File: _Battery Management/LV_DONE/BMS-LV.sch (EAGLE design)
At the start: 114 parts, among them J1 M1x5, J2 M1x4, J3 M1x4, J4 M1x4, J5 M1x2, J6 MX150L, J8 M1x5, J9 M80022232081-2, K1 ADJ14024, Q2 40V 0.2A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

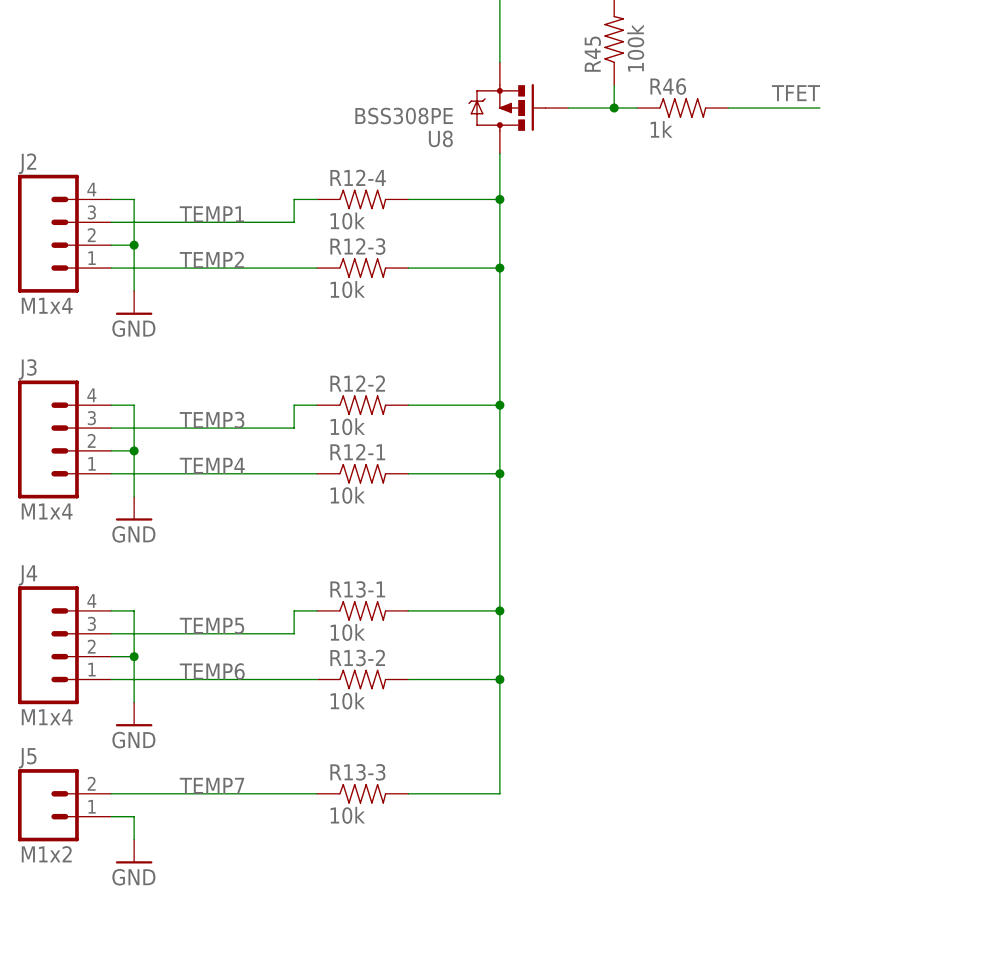
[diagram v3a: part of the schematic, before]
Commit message: Fixing layout issues.
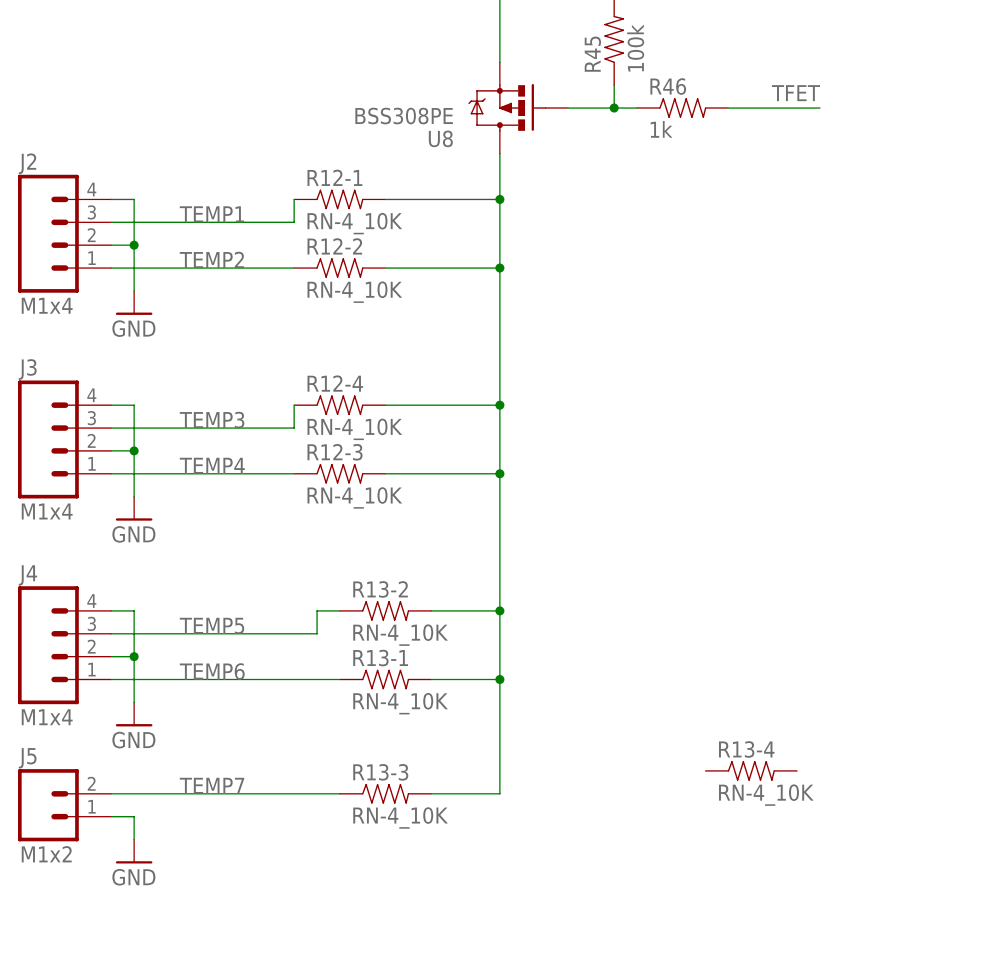
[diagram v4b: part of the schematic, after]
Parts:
- R12, R13: value 10k -> RN-4_10K
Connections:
- net TEMP1: now also R12-1.1; no longer R12-4.1
- net TEMP2: now also R12-2.1; no longer R12-3.1
- net TEMP3: now also R12-4.1; no longer R12-2.1
- net TEMP4: now also R12-3.1; no longer R12-1.1
- net TEMP5: now also R13-2.1; no longer R13-1.1
- net TEMP6: now also R13-1.1; no longer R13-2.1
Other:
- moved on the sheet: R12-1, R12-2, R12-3, R12-4, R13-1, R13-2, R13-3
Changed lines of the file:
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@@
 <part name="J3" library="FSAE Electric" deviceset="M4" device="_1X4_LOCK" value="M1x4"/>
 <part name="J4" library="FSAE Electric" deviceset="M4" device="_1X4_LOCK" value="M1x4"/>
-<part name="R13" library="FSAE Electric" deviceset="RN-4" device="_10K" value="10k"/>
 <part name="GND6" library="supply1" deviceset="GND" device=""/>
 <part name="GND16" library="supply1" deviceset="GND" device=""/>
@@
 <part name="J6" library="FSAE Electric" deviceset="M2X3" device="MX150L" value="MX150L"/>
 <part name="C1" library="FSAE Electric" deviceset="CAP" device="_0.1UF_50V" value="0.1uF"/>
-<part name="R12" library="FSAE Electric" deviceset="RN-4" device="_10K" value="10k"/>
 <part name="J9" library="FSAE Electric" deviceset="M8" device="0022232081-2"/>
 <part name="R50" library="FSAE Electric" deviceset="RES" device="_4.99K_1%" value="4.99k"/>
@@
 <part name="R58" library="FSAE Electric" deviceset="RES" device="_10K_1%" value="10k"/>
 <part name="P+4" library="supply1" deviceset="+5V" device=""/>
+<part name="R12" library="FSAE Electric" deviceset="RN-4" device="_10K"/>
+<part name="R13" library="FSAE Electric" deviceset="RN-4" device="_10K"/>
 </parts>
 <sheets>
@@
 <instance part="J3" gate="G$1" x="22.86" y="68.58"/>
 <instance part="J4" gate="G$1" x="22.86" y="45.72"/>
-<instance part="R13" gate="-1" x="55.88" y="45.72"/>
-<instance part="R13" gate="-2" x="55.88" y="38.1"/>
-<instance part="R13" gate="-3" x="55.88" y="25.4"/>
 <instance part="GND6" gate="1" x="30.48" y="78.74"/>
 <instance part="GND16" gate="1" x="30.48" y="55.88"/>
@@
 <attribute name="VALUE" x="55.88" y="243.84" size="1.778" layer="96"/>
 </instance>
-<instance part="R12" gate="-1" x="55.88" y="60.96"/>
-<instance part="R12" gate="-2" x="55.88" y="68.58"/>
-<instance part="R12" gate="-3" x="55.88" y="83.82"/>
-<instance part="R12" gate="-4" x="55.88" y="91.44"/>
 <instance part="J9" gate="G$1" x="231.14" y="177.8"/>
 <instance part="R50" gate="G$1" x="441.96" y="200.66" rot="R90"/>
@@
 <attribute name="VALUE" x="462.28" y="182.88" size="1.778" layer="96" rot="R90"/>
 </instance>
+<instance part="R12" gate="-1" x="53.34" y="91.44"/>
+<instance part="R12" gate="-2" x="53.34" y="83.82"/>
+<instance part="R12" gate="-3" x="53.34" y="60.96"/>
+<instance part="R12" gate="-4" x="53.34" y="68.58"/>
+<instance part="R13" gate="-1" x="58.42" y="38.1"/>
+<instance part="R13" gate="-2" x="58.42" y="45.72"/>
+<instance part="R13" gate="-3" x="58.42" y="25.4"/>
+<instance part="R13" gate="-4" x="99.06" y="27.94"/>
 </instances>
 <busses>
@@
 </segment>
 <segment>
-<wire x1="50.8" y1="91.44" x2="48.26" y2="91.44" width="0.1524" layer="91"/>
-<wire x1="48.26" y1="91.44" x2="48.26" y2="88.9" width="0.1524" layer="91"/>
 <pinref part="J2" gate="G$1" pin="3"/>
 <wire x1="48.26" y1="88.9" x2="27.94" y2="88.9" width="0.1524" layer="91"/>
 <label x="35.56" y="88.9" size="1.778" layer="95"/>
-<pinref part="R12" gate="-4" pin="1"/>
+<pinref part="R12" gate="-1" pin="1"/>
+<wire x1="48.26" y1="88.9" x2="48.26" y2="91.44" width="0.1524" layer="91"/>
 </segment>
 </net>
@@
 </segment>
 <segment>
-<wire x1="50.8" y1="68.58" x2="48.26" y2="68.58" width="0.1524" layer="91"/>
-<wire x1="48.26" y1="68.58" x2="48.26" y2="66.04" width="0.1524" layer="91"/>
 <pinref part="J3" gate="G$1" pin="3"/>
 <wire x1="48.26" y1="66.04" x2="27.94" y2="66.04" width="0.1524" layer="91"/>
 <label x="35.56" y="66.04" size="1.778" layer="95"/>
-<pinref part="R12" gate="-2" pin="1"/>
+<pinref part="R12" gate="-4" pin="1"/>
+<wire x1="48.26" y1="66.04" x2="48.26" y2="68.58" width="0.1524" layer="91"/>
 </segment>
 </net>
@@
 </segment>
 <segment>
-<wire x1="48.26" y1="45.72" x2="48.26" y2="43.18" width="0.1524" layer="91"/>
 <pinref part="J4" gate="G$1" pin="3"/>
-<wire x1="48.26" y1="43.18" x2="27.94" y2="43.18" width="0.1524" layer="91"/>
+<wire x1="50.8" y1="45.72" x2="50.8" y2="43.18" width="0.1524" layer="91"/>
+<wire x1="50.8" y1="43.18" x2="27.94" y2="43.18" width="0.1524" layer="91"/>
 <label x="35.56" y="43.18" size="1.778" layer="95"/>
-<pinref part="R13" gate="-1" pin="1"/>
-<wire x1="48.26" y1="45.72" x2="50.8" y2="45.72" width="0.1524" layer="91"/>
+<pinref part="R13" gate="-2" pin="1"/>
+<wire x1="50.8" y1="45.72" x2="53.34" y2="45.72" width="0.1524" layer="91"/>
 </segment>
 </net>
@@
 <segment>
 <pinref part="J2" gate="G$1" pin="1"/>
-<wire x1="50.8" y1="83.82" x2="27.94" y2="83.82" width="0.1524" layer="91"/>
+<wire x1="48.26" y1="83.82" x2="27.94" y2="83.82" width="0.1524" layer="91"/>
 <label x="35.56" y="83.82" size="1.778" layer="95"/>
-<pinref part="R12" gate="-3" pin="1"/>
+<pinref part="R12" gate="-2" pin="1"/>
 </segment>
 </net>
@@
 <segment>
 <pinref part="J3" gate="G$1" pin="1"/>
-<wire x1="50.8" y1="60.96" x2="27.94" y2="60.96" width="0.1524" layer="91"/>
+<wire x1="48.26" y1="60.96" x2="27.94" y2="60.96" width="0.1524" layer="91"/>
 <label x="35.56" y="60.96" size="1.778" layer="95"/>
-<pinref part="R12" gate="-1" pin="1"/>
+<pinref part="R12" gate="-3" pin="1"/>
 </segment>
 </net>
@@
 </segment>
 <segment>
-<pinref part="R13" gate="-2" pin="1"/>
 <pinref part="J4" gate="G$1" pin="1"/>
-<wire x1="50.8" y1="38.1" x2="27.94" y2="38.1" width="0.1524" layer="91"/>
+<wire x1="53.34" y1="38.1" x2="27.94" y2="38.1" width="0.1524" layer="91"/>
 <label x="35.56" y="38.1" size="1.778" layer="95"/>
+<pinref part="R13" gate="-1" pin="1"/>
 </segment>
 </net>
 <net name="N$78" class="0">
 <segment>
-<wire x1="60.96" y1="91.44" x2="71.12" y2="91.44" width="0.1524" layer="91"/>
+<pinref part="U8" gate="G$1" pin="D"/>
+<wire x1="71.12" y1="25.4" x2="71.12" y2="38.1" width="0.1524" layer="91"/>
+<wire x1="71.12" y1="38.1" x2="71.12" y2="45.72" width="0.1524" layer="91"/>
+<wire x1="71.12" y1="45.72" x2="71.12" y2="60.96" width="0.1524" layer="91"/>
+<wire x1="71.12" y1="60.96" x2="71.12" y2="68.58" width="0.1524" layer="91"/>
+<wire x1="71.12" y1="68.58" x2="71.12" y2="83.82" width="0.1524" layer="91"/>
+<wire x1="71.12" y1="83.82" x2="71.12" y2="91.44" width="0.1524" layer="91"/>
 <wire x1="71.12" y1="91.44" x2="71.12" y2="96.52" width="0.1524" layer="91"/>
-<wire x1="60.96" y1="83.82" x2="71.12" y2="83.82" width="0.1524" layer="91"/>
-<wire x1="71.12" y1="83.82" x2="71.12" y2="91.44" width="0.1524" layer="91"/>
-<wire x1="60.96" y1="68.58" x2="71.12" y2="68.58" width="0.1524" layer="91"/>
-<wire x1="71.12" y1="68.58" x2="71.12" y2="83.82" width="0.1524" layer="91"/>
-<wire x1="60.96" y1="60.96" x2="71.12" y2="60.96" width="0.1524" layer="91"/>
-<wire x1="71.12" y1="60.96" x2="71.12" y2="68.58" width="0.1524" layer="91"/>
+<pinref part="R12" gate="-1" pin="2"/>
+<wire x1="58.42" y1="91.44" x2="71.12" y2="91.44" width="0.1524" layer="91"/>
+<pinref part="R12" gate="-2" pin="2"/>
+<wire x1="58.42" y1="83.82" x2="71.12" y2="83.82" width="0.1524" layer="91"/>
+<junction x="71.12" y="91.44"/>
+<junction x="71.12" y="83.82"/>
+<pinref part="R12" gate="-4" pin="2"/>
+<wire x1="58.42" y1="68.58" x2="71.12" y2="68.58" width="0.1524" layer="91"/>
+<pinref part="R12" gate="-3" pin="2"/>
+<wire x1="58.42" y1="60.96" x2="71.12" y2="60.96" width="0.1524" layer="91"/>
+<junction x="71.12" y="68.58"/>
 <junction x="71.12" y="60.96"/>
-<junction x="71.12" y="68.58"/>
-<junction x="71.12" y="83.82"/>
-<junction x="71.12" y="91.44"/>
-<wire x1="71.12" y1="45.72" x2="71.12" y2="60.96" width="0.1524" layer="91"/>
-<wire x1="71.12" y1="25.4" x2="71.12" y2="38.1" width="0.1524" layer="91"/>
-<pinref part="U8" gate="G$1" pin="D"/>
-<pinref part="R12" gate="-1" pin="2"/>
-<pinref part="R12" gate="-2" pin="2"/>
-<pinref part="R12" gate="-3" pin="2"/>
-<pinref part="R12" gate="-4" pin="2"/>
-<wire x1="71.12" y1="38.1" x2="71.12" y2="45.72" width="0.1524" layer="91"/>
+<pinref part="R13" gate="-3" pin="2"/>
+<wire x1="63.5" y1="25.4" x2="71.12" y2="25.4" width="0.1524" layer="91"/>
+<pinref part="R13" gate="-2" pin="2"/>
+<wire x1="63.5" y1="45.72" x2="71.12" y2="45.72" width="0.1524" layer="91"/>
 <pinref part="R13" gate="-1" pin="2"/>
-<wire x1="60.96" y1="45.72" x2="71.12" y2="45.72" width="0.1524" layer="91"/>
+<wire x1="63.5" y1="38.1" x2="71.12" y2="38.1" width="0.1524" layer="91"/>
 <junction x="71.12" y="45.72"/>
-<pinref part="R13" gate="-2" pin="2"/>
-<wire x1="60.96" y1="38.1" x2="71.12" y2="38.1" width="0.1524" layer="91"/>
 <junction x="71.12" y="38.1"/>
-<wire x1="60.96" y1="25.4" x2="71.12" y2="25.4" width="0.1524" layer="91"/>
-<pinref part="R13" gate="-3" pin="2"/>
 </segment>
 </net>
@@
 </segment>
 <segment>
+<pinref part="J5" gate="G$1" pin="2"/>
+<wire x1="53.34" y1="25.4" x2="27.94" y2="25.4" width="0.1524" layer="91"/>
+<label x="35.56" y="25.4" size="1.778" layer="95"/>
 <pinref part="R13" gate="-3" pin="1"/>
-<pinref part="J5" gate="G$1" pin="2"/>
-<wire x1="50.8" y1="25.4" x2="27.94" y2="25.4" width="0.1524" layer="91"/>
-<label x="35.56" y="25.4" size="1.778" layer="95"/>
-</segment>
-</net>
+</segment>
+</net>
